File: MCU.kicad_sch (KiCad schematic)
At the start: 11 parts, among them J1 Conn_ARM_JTAG_SWD_10, U1 STM32H725ZGT6, U2 M95P32-IXMNT_E, Y1 ABS05W-32.768KHZ-D-2-T, Y2 ECS-80-8-30Q-VY-TR

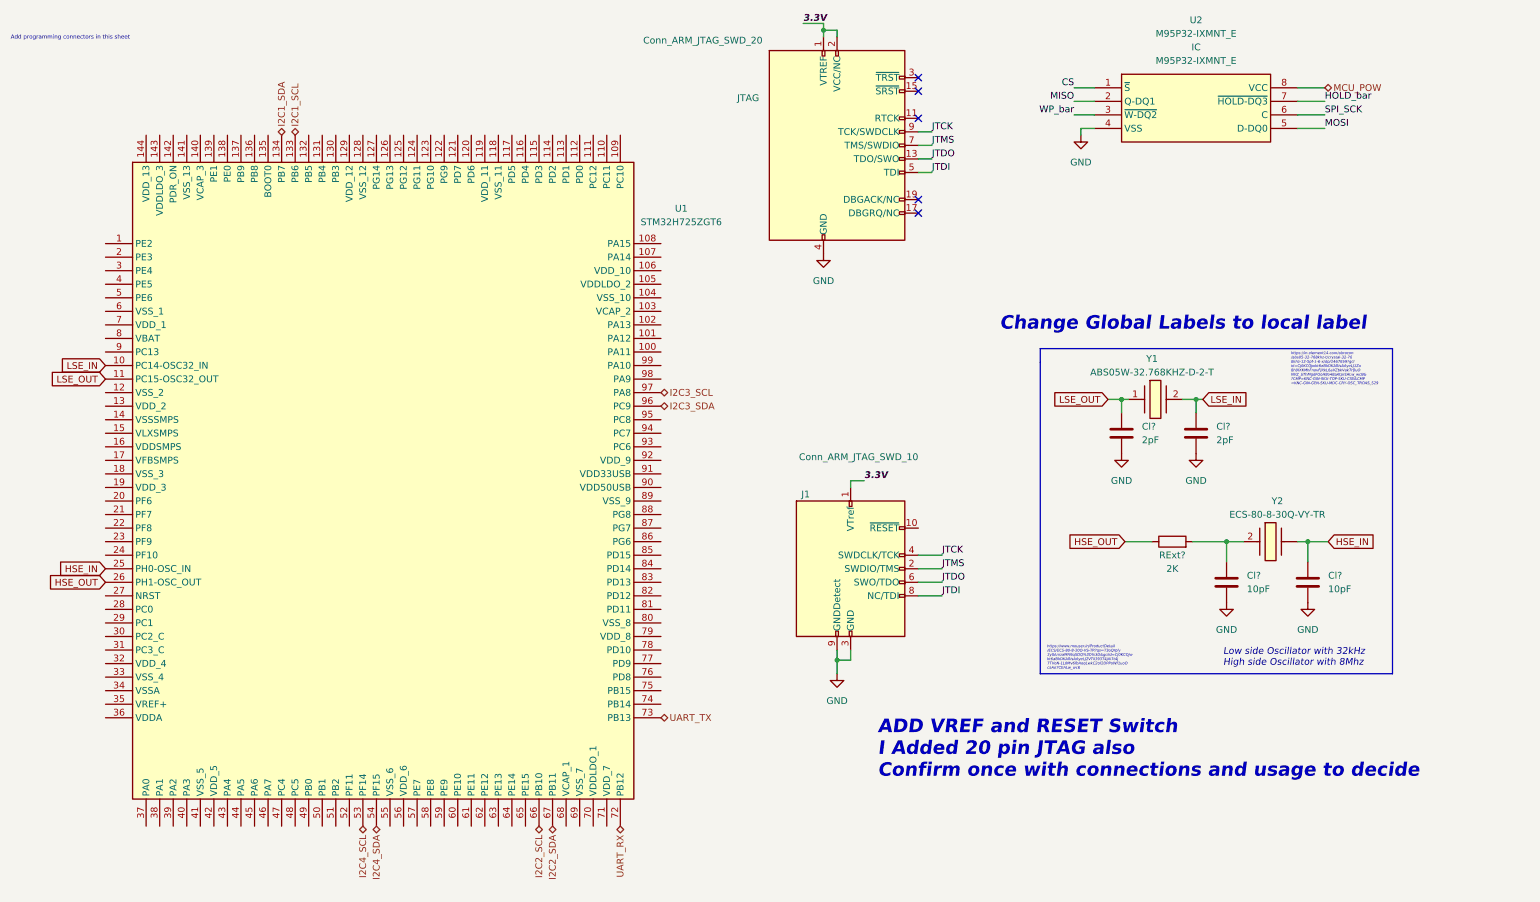
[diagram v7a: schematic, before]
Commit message: Reset switch added
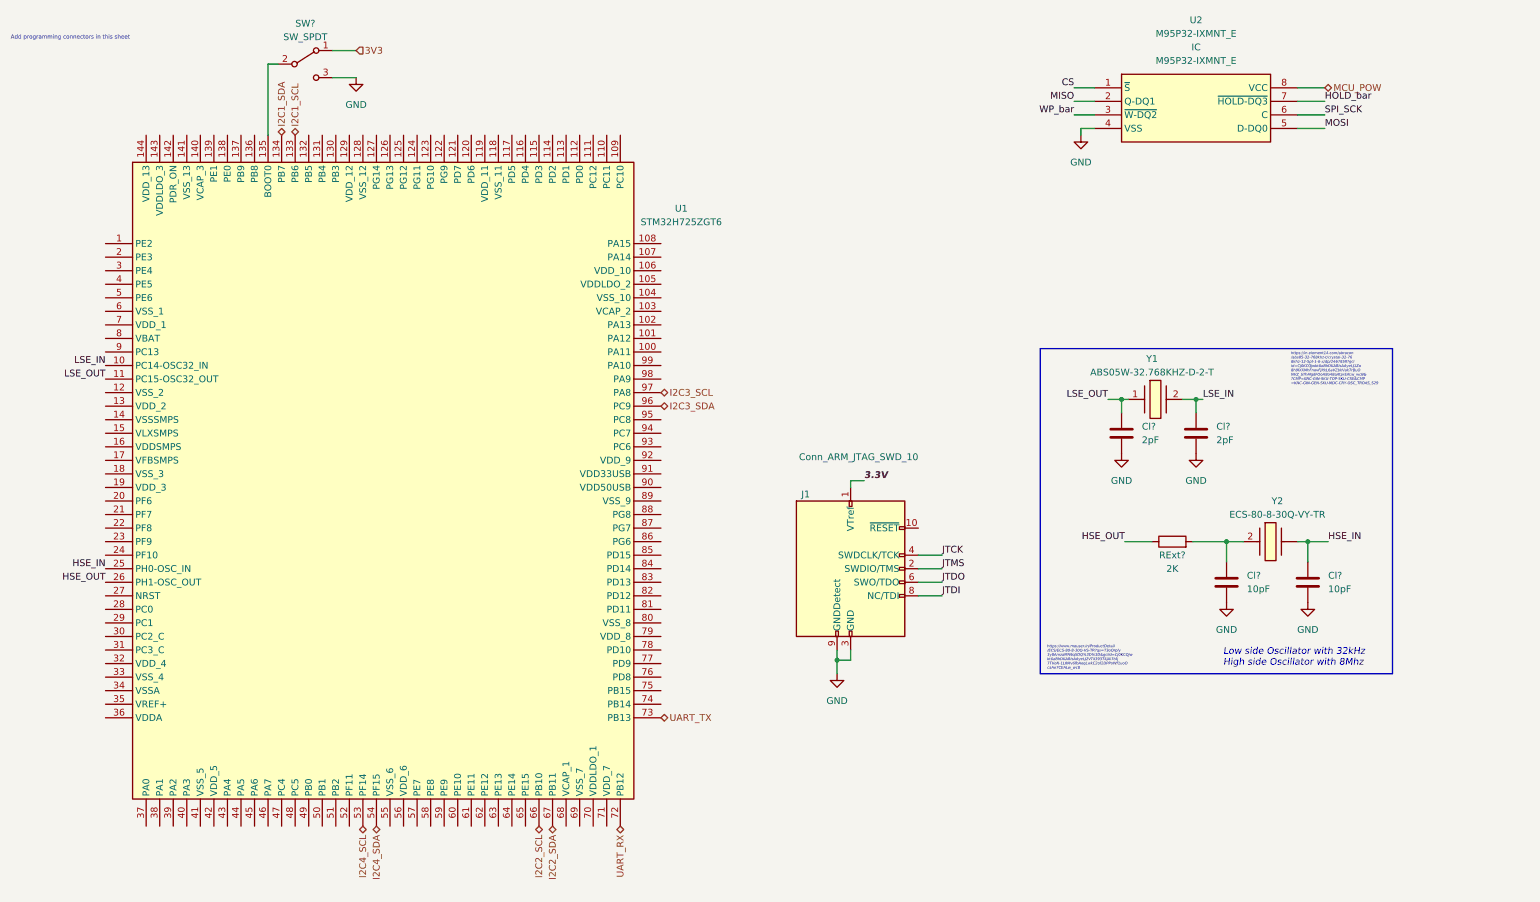
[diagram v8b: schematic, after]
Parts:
- removed JTAG: Conn_ARM_JTAG_SWD_20, symbol Connector:Conn_ARM_JTAG_SWD_20
- added SW?: SW_SPDT, symbol Switch:SW_SPDT
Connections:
- net GND: now also SW?.3 (C)
- net at U1.135 (BOOT0): now also SW?.2 (B)
- new net 3V3: SW?.1 (A)
- no-connect marks 5 -> 0
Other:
- note removed: "ADD VREF and RESET Switch I Added 20 pin JTAG also Confirm once with connections and usage to decide"
- note removed: "Change Global Labels to local label"
